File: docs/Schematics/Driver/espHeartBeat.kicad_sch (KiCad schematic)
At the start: 0 parts

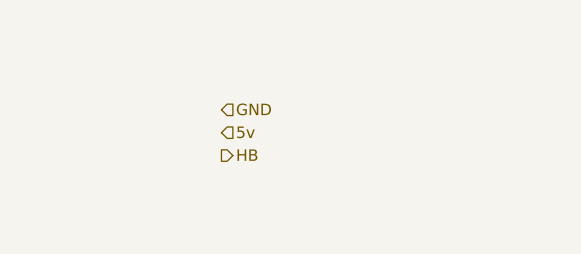
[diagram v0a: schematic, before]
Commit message: First scematic design for the card
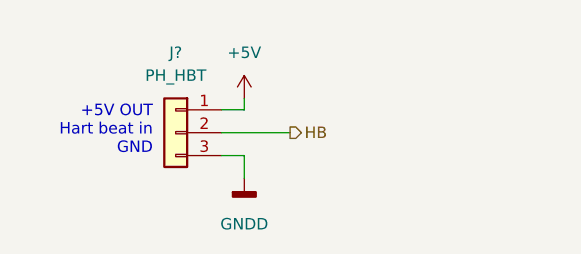
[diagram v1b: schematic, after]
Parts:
- added J?: PH_HBT, symbol Connector_Generic:Conn_01x03
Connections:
- net HB: now also J?.2 (Pin_2)
- new net +5V: J?.1 (Pin_1)
- new net GNDD: J?.3 (Pin_3)
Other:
- note added: "+5V OUT Hart beat in GND"
- company: (none) -> HiQ
- title: (none) -> Arty Z7 IO expander card
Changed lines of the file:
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@@
 (kicad_sch (version 20211123) (generator eeschema)
   (paper "A4")
-  (hierarchical_label "HB" (shape output) (at 179.07 86.36 0)
+  (title_block
+    (title "Arty Z7 IO expander card")
+    (date "2022-12-24")
+    (rev "0.1")
+    (company "HiQ")
+  )
+  (wire (pts (xy 179.07 86.36) (xy 181.61 86.36))
+    (stroke (width 0) (type default) (color 0 0 0 0))
+  )
+  (wire (pts (xy 181.61 80.01) (xy 181.61 81.28))
+    (stroke (width 0) (type default) (color 0 0 0 0))
+  )
+  (wire (pts (xy 186.69 83.82) (xy 179.07 83.82))
+    (stroke (width 0) (type default) (color 0 0 0 0))
+  )
+  (wire (pts (xy 181.61 86.36) (xy 181.61 88.9))
+    (stroke (width 0) (type default) (color 0 0 0 0))
+  )
+  (wire (pts (xy 179.07 81.28) (xy 181.61 81.28))
+    (stroke (width 0) (type default) (color 0 0 0 0))
+  )
+  (text "+5V OUT\nHart beat in\nGND" (at 171.45 86.36 180)
+    (effects (font (size 1.27 1.27)) (justify right bottom))
+  )
+  (hierarchical_label "HB" (shape output) (at 186.69 83.82 0)
     (effects (font (size 1.27 1.27)) (justify left))
   )
-  (hierarchical_label "GND" (shape input) (at 179.07 81.28 0)
-    (effects (font (size 1.27 1.27)) (justify left))
+  (symbol (lib_id "power:+5V") (at 181.61 80.01 0) (unit 1)
+    (in_bom yes) (on_board yes) (fields_autoplaced)
+    (property "Reference" "#PWR?" (id 0) (at 181.61 83.82 0)
+      (effects (font (size 1.27 1.27)) hide)
+    )
+    (property "Value" "+5V" (id 1) (at 181.61 74.93 0))
+    (property "Footprint" "" (id 2) (at 181.61 80.01 0)
+      (effects (font (size 1.27 1.27)) hide)
+    )
+    (property "Datasheet" "" (id 3) (at 181.61 80.01 0)
+      (effects (font (size 1.27 1.27)) hide)
+    )
+    (pin "1")
   )
-  (hierarchical_label "5v" (shape input) (at 179.07 83.82 0)
-    (effects (font (size 1.27 1.27)) (justify left))
+  (symbol (lib_id "Connector_Generic:Conn_01x03") (at 173.99 83.82 0) (mirror y) (unit 1)
+    (in_bom yes) (on_board yes) (fields_autoplaced)
+    (property "Reference" "J?" (id 0) (at 173.99 74.93 0))
+    (property "Value" "PH_HBT" (id 1) (at 173.99 77.47 0))
+    (property "Footprint" "" (id 2) (at 173.99 83.82 0)
+      (effects (font (size 1.27 1.27)) hide)
+    )
+    (property "Datasheet" "~" (id 3) (at 173.99 83.82 0)
+      (effects (font (size 1.27 1.27)) hide)
+    )
+    (pin "1")
+    (pin "2")
+    (pin "3")
+  )
+  (symbol (lib_id "power:GNDD") (at 181.61 88.9 0) (unit 1)
+    (in_bom yes) (on_board yes) (fields_autoplaced)
+    (property "Reference" "#PWR?" (id 0) (at 181.61 95.25 0)
+      (effects (font (size 1.27 1.27)) hide)
+    )
+    (property "Value" "GNDD" (id 1) (at 181.61 93.98 0))
+    (property "Footprint" "" (id 2) (at 181.61 88.9 0)
+      (effects (font (size 1.27 1.27)) hide)
+    )
+    (property "Datasheet" "" (id 3) (at 181.61 88.9 0)
+      (effects (font (size 1.27 1.27)) hide)
+    )
+    (pin "1")
   )
 )

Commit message: Added footprints and a symbol for the level shifters
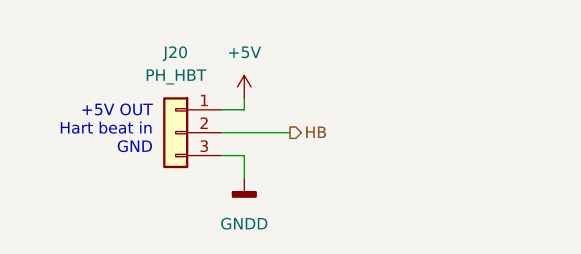
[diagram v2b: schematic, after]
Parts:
- J20: renamed from J?; footprint (none) -> Connector_PinHeader_2.54mm:PinHeader_1x03_P2.54mm_Vertical
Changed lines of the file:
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@@
   (symbol (lib_id "power:+5V") (at 181.61 80.01 0) (unit 1)
     (in_bom yes) (on_board yes) (fields_autoplaced)
-    (property "Reference" "#PWR?" (id 0) (at 181.61 83.82 0)
+    (property "Reference" "#PWR048" (id 0) (at 181.61 83.82 0)
       (effects (font (size 1.27 1.27)) hide)
     )
@@
   (symbol (lib_id "Connector_Generic:Conn_01x03") (at 173.99 83.82 0) (mirror y) (unit 1)
     (in_bom yes) (on_board yes) (fields_autoplaced)
-    (property "Reference" "J?" (id 0) (at 173.99 74.93 0))
+    (property "Reference" "J20" (id 0) (at 173.99 74.93 0))
     (property "Value" "PH_HBT" (id 1) (at 173.99 77.47 0))
-    (property "Footprint" "" (id 2) (at 173.99 83.82 0)
+    (property "Footprint" "Connector_PinHeader_2.54mm:PinHeader_1x03_P2.54mm_Vertical" (id 2) (at 173.99 83.82 0)
       (effects (font (size 1.27 1.27)) hide)
     )
@@
   (symbol (lib_id "power:GNDD") (at 181.61 88.9 0) (unit 1)
     (in_bom yes) (on_board yes) (fields_autoplaced)
-    (property "Reference" "#PWR?" (id 0) (at 181.61 95.25 0)
+    (property "Reference" "#PWR049" (id 0) (at 181.61 95.25 0)
       (effects (font (size 1.27 1.27)) hide)
     )

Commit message: Added caps and changed the connection from the motor sensors to plints
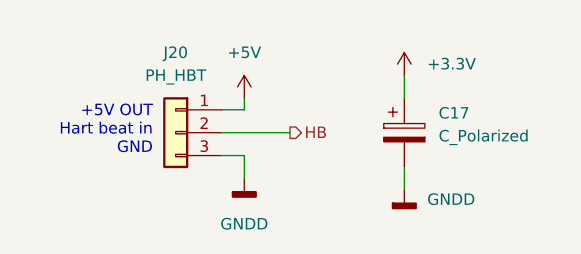
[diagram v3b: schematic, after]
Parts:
- added C17: C_Polarized, Capacitor_THT:CP_Radial_D8.0mm_P3.80mm, symbol Device:C_Polarized
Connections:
- net GNDD: now also C17.2
- new net +3.3V: C17.1
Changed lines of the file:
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@@
+    (stroke (width 0) (type default) (color 0 0 0 0))
+  )
+  (wire (pts (xy 199.39 87.63) (xy 199.39 90.17))
     (stroke (width 0) (type default) (color 0 0 0 0))
   )
   (wire (pts (xy 179.07 81.28) (xy 181.61 81.28))
+    (stroke (width 0) (type default) (color 0 0 0 0))
+  )
+  (wire (pts (xy 199.39 77.47) (xy 199.39 80.01))
     (stroke (width 0) (type default) (color 0 0 0 0))
   )
@@
     (pin "3")
   )
+  (symbol (lib_id "power:+3.3V") (at 199.39 77.47 0) (unit 1)
+    (in_bom yes) (on_board yes) (fields_autoplaced)
+    (property "Reference" "#PWR093" (id 0) (at 199.39 81.28 0)
+      (effects (font (size 1.27 1.27)) hide)
+    )
+    (property "Value" "+3.3V" (id 1) (at 201.93 76.1999 0)
+      (effects (font (size 1.27 1.27)) (justify left))
+    )
+    (property "Footprint" "" (id 2) (at 199.39 77.47 0)
+      (effects (font (size 1.27 1.27)) hide)
+    )
+    (property "Datasheet" "" (id 3) (at 199.39 77.47 0)
+      (effects (font (size 1.27 1.27)) hide)
+    )
+    (pin "1")
+  )
   (symbol (lib_id "power:GNDD") (at 181.61 88.9 0) (unit 1)
     (in_bom yes) (on_board yes) (fields_autoplaced)
@@
     (pin "1")
   )
+  (symbol (lib_id "power:GNDD") (at 199.39 90.17 0) (unit 1)
+    (in_bom yes) (on_board yes) (fields_autoplaced)
+    (property "Reference" "#PWR094" (id 0) (at 199.39 96.52 0)
+      (effects (font (size 1.27 1.27)) hide)
+    )
+    (property "Value" "GNDD" (id 1) (at 201.93 91.2494 0)
+      (effects (font (size 1.27 1.27)) (justify left))
+    )
+    (property "Footprint" "" (id 2) (at 199.39 90.17 0)
+      (effects (font (size 1.27 1.27)) hide)
+    )
+    (property "Datasheet" "" (id 3) (at 199.39 90.17 0)
+      (effects (font (size 1.27 1.27)) hide)
+    )
+    (pin "1")
+  )
+  (symbol (lib_id "Device:C_Polarized") (at 199.39 83.82 0) (unit 1)
+    (in_bom yes) (on_board yes) (fields_autoplaced)
+    (property "Reference" "C17" (id 0) (at 203.2 81.6609 0)
+      (effects (font (size 1.27 1.27)) (justify left))
+    )
+    (property "Value" "C_Polarized" (id 1) (at 203.2 84.2009 0)
+      (effects (font (size 1.27 1.27)) (justify left))
+    )
+    (property "Footprint" "Capacitor_THT:CP_Radial_D8.0mm_P3.80mm" (id 2) (at 200.3552 87.63 0)
+      (effects (font (size 1.27 1.27)) hide)
+    )
+    (property "Datasheet" "~" (id 3) (at 199.39 83.82 0)
+      (effects (font (size 1.27 1.27)) hide)
+    )
+    (pin "1")
+    (pin "2")
+  )
 )

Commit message: Started routing the pcb.
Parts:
- C17: footprint Capacitor_THT:CP_Radial_D8.0mm_P3.80mm -> Capacitor_SMD:C_0805_2012Metric_Pad1.18x1.45mm_HandSolder
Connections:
- net +3.3V is gone; now on net +5V: C17.1
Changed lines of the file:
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@@
     (pin "3")
-  )
-  (symbol (lib_id "power:+3.3V") (at 199.39 77.47 0) (unit 1)
-    (in_bom yes) (on_board yes) (fields_autoplaced)
-    (property "Reference" "#PWR093" (id 0) (at 199.39 81.28 0)
-      (effects (font (size 1.27 1.27)) hide)
-    )
-    (property "Value" "+3.3V" (id 1) (at 201.93 76.1999 0)
-      (effects (font (size 1.27 1.27)) (justify left))
-    )
-    (property "Footprint" "" (id 2) (at 199.39 77.47 0)
-      (effects (font (size 1.27 1.27)) hide)
-    )
-    (property "Datasheet" "" (id 3) (at 199.39 77.47 0)
-      (effects (font (size 1.27 1.27)) hide)
-    )
-    (pin "1")
   )
   (symbol (lib_id "power:GNDD") (at 181.61 88.9 0) (unit 1)
@@
     )
     (property "Datasheet" "" (id 3) (at 181.61 88.9 0)
+      (effects (font (size 1.27 1.27)) hide)
+    )
+    (pin "1")
+  )
+  (symbol (lib_id "power:+5V") (at 199.39 77.47 0) (unit 1)
+    (in_bom yes) (on_board yes) (fields_autoplaced)
+    (property "Reference" "#PWR0102" (id 0) (at 199.39 81.28 0)
+      (effects (font (size 1.27 1.27)) hide)
+    )
+    (property "Value" "+5V" (id 1) (at 199.39 72.39 0))
+    (property "Footprint" "" (id 2) (at 199.39 77.47 0)
+      (effects (font (size 1.27 1.27)) hide)
+    )
+    (property "Datasheet" "" (id 3) (at 199.39 77.47 0)
       (effects (font (size 1.27 1.27)) hide)
     )
@@
       (effects (font (size 1.27 1.27)) (justify left))
     )
-    (property "Footprint" "Capacitor_THT:CP_Radial_D8.0mm_P3.80mm" (id 2) (at 200.3552 87.63 0)
+    (property "Footprint" "Capacitor_SMD:C_0805_2012Metric_Pad1.18x1.45mm_HandSolder" (id 2) (at 200.3552 87.63 0)
       (effects (font (size 1.27 1.27)) hide)
     )

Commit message: First version of the routed board is done
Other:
- title: Arty Z7 IO expander card -> Arty Z7 IO Board
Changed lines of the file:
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@@
   (paper "A4")
   (title_block
-    (title "Arty Z7 IO expander card")
+    (title "Arty Z7 IO Board")
     (date "2022-12-24")
-    (rev "0.1")
+    (rev "${VER}")
     (company "HiQ")
   )
